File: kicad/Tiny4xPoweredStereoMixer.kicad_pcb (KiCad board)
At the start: 2 copper layers, 45 parts, among them J1 RCJ-2221, J2 RCJ-2221, J3 RCJ-2221, J4 RCJ-2221, J5 RCJ-2221, U1 TL072, U2 TL072, U3 TL072, U4 TL072, U5 TL072, U6 LM2611AMF/NOPB

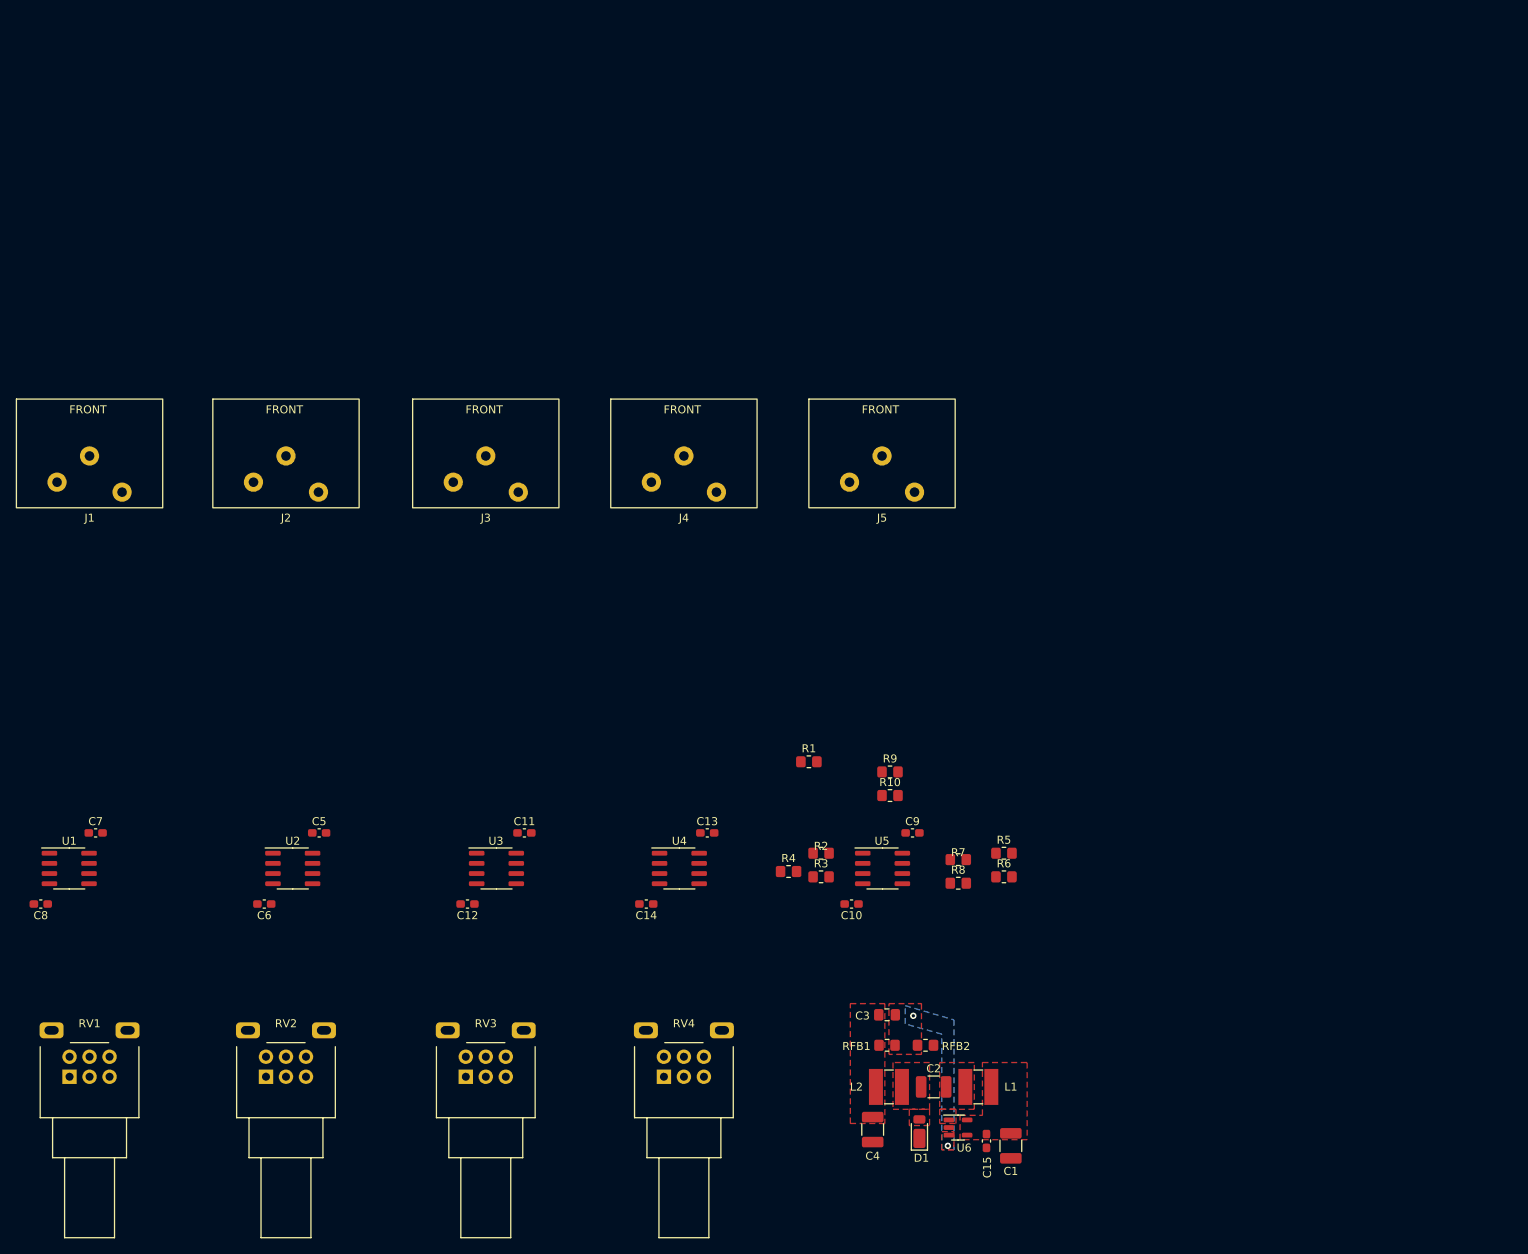
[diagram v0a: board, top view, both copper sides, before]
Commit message: positioned +/-12v connectors
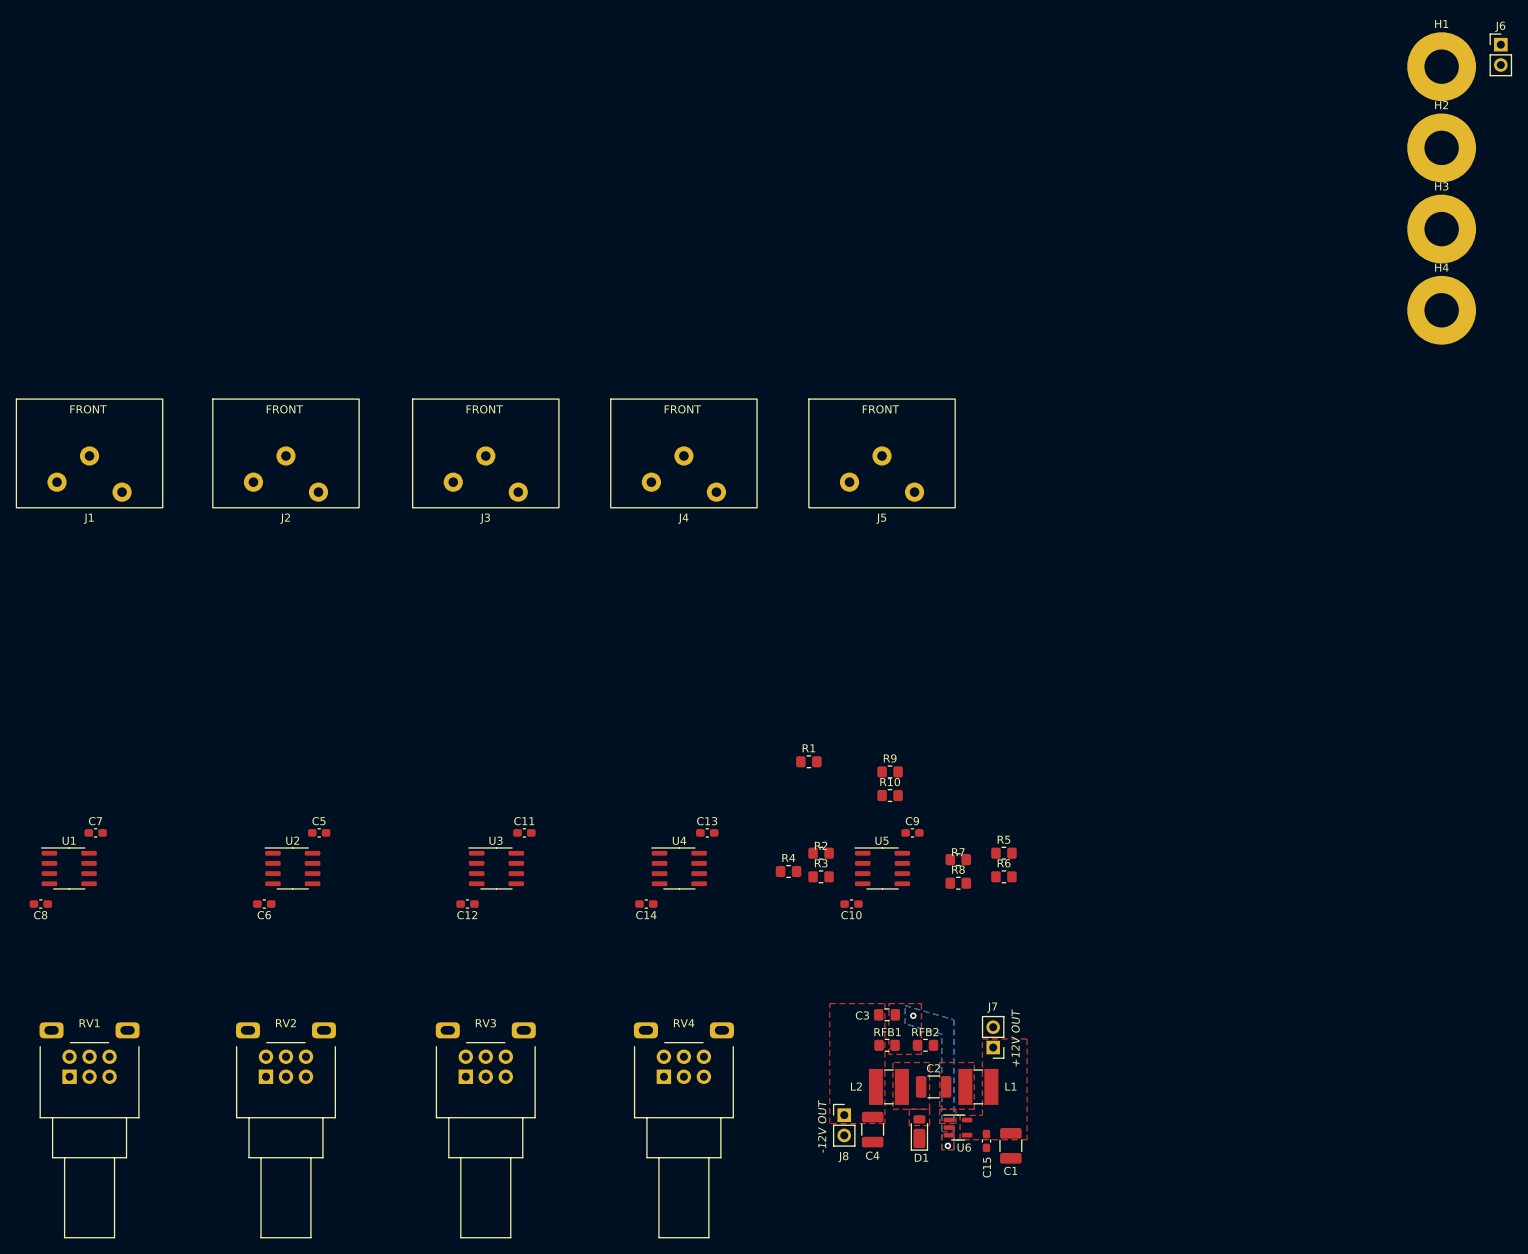
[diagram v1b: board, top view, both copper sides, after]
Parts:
- added H1: MountingHole, MountingHole:MountingHole_4.3mm_M4_Pad, F.Cu at (247.8, 23.6)
- added H2: MountingHole, MountingHole:MountingHole_4.3mm_M4_Pad, F.Cu at (247.8, 33.8)
- added H3: MountingHole, MountingHole:MountingHole_4.3mm_M4_Pad, F.Cu at (247.8, 43.9)
- added H4: MountingHole, MountingHole:MountingHole_4.3mm_M4_Pad, F.Cu at (247.8, 54.1)
- added J6: PowerConnector, Connector_PinHeader_2.54mm:PinHeader_1x02_P2.54mm_Vertical, F.Cu at (255.2, 20.9)
- added J7: PowerConnector, Connector_PinHeader_2.54mm:PinHeader_1x02_P2.54mm_Vertical, F.Cu at (191.7, 146.2)
- added J8: PowerConnector, Connector_PinHeader_2.54mm:PinHeader_1x02_P2.54mm_Vertical, F.Cu at (173.1, 154.7)
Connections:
- C1 pad 2: +12V -> Net-(J6-Pin_2)
- C15 pad 1: +12V -> Net-(J6-Pin_2)
- C3 pad 2: -12V -> Net-(J8-Pin_1)
- C4 pad 2: -12V -> Net-(J8-Pin_1)
- L1 pad 1: +12V -> Net-(J6-Pin_2)
- L2 pad 2: -12V -> Net-(J8-Pin_1)
- RFB1 pad 1: -12V -> Net-(J8-Pin_1)
- U6 pad 4: +12V -> Net-(J6-Pin_2)
- U6 pad 5: +12V -> Net-(J6-Pin_2)
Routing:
- added copper zone on F.Cu, net Net-(J6-Pin_2)
- added copper zone on F.Cu, net Net-(J8-Pin_1)
- removed copper zone on F.Cu, net +12V
- removed copper zone on F.Cu, net -12V

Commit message: completed reva layout
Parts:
- H1, H2, H3, H4: footprint MountingHole:MountingHole_4.3mm_M4_Pad -> MountingHole:MountingHole_3mm
- J1, J2, J3, J4, J5: footprint RCAJack:RCJ-22 -> RCAJack:CUI_DEVICES_RCJ-2211
- RV1, RV2, RV3, RV4: footprint Potentiometer_THT:Potentiometer_Alps_RK09L_Double_Horizontal -> Potentiometers:Potentiometer_Alps_RK09L_Double_Horizontal
- moved H2 180.1 mm to (100.3, 137.2)
- moved H3 163.4 mm to (104.1, 121.9)
- moved J6 154.8 mm to (170.4, 150.4), turned to 90 degrees
- moved H1 145.9 mm to (156.2, 137.2)
- moved H4 124.4 mm to (143.5, 121.9)
- moved J1 37.3 mm to (93.8, 105.3)
- moved J2 35.7 mm to (113.5, 105.3)
- moved J5 34.5 mm to (172.7, 105.3)
- moved J3 34.5 mm to (133.3, 105.3)
- moved J4 34.2 mm to (153.0, 105.3)
- moved R6 27.6 mm to (165.8, 120.1)
- moved R5 27.2 mm to (165.8, 122.4)
- moved C8 24.8 mm to (97.0, 123.2), turned to 0 degrees
- moved R8 23.7 mm to (165.8, 115.6)
- moved J8 22.3 mm to (161.9, 135.4), turned to 180 degrees
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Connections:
- R1 pad 1: /BufferOpAmp1/left_channel_buffered -> /BufferOpAmp4/left_channel_buffered
- R2 pad 1: /BufferOpAmp2/left_channel_buffered -> /BufferOpAmp3/left_channel_buffered
- R3 pad 1: /BufferOpAmp3/left_channel_buffered -> /BufferOpAmp2/left_channel_buffered
- R4 pad 1: /BufferOpAmp4/left_channel_buffered -> /BufferOpAmp1/left_channel_buffered
- R5 pad 1: /BufferOpAmp1/right_channel_buffered -> /BufferOpAmp4/right_channel_buffered
- R6 pad 1: /BufferOpAmp2/right_channel_buffered -> /BufferOpAmp3/right_channel_buffered
- R7 pad 1: /BufferOpAmp3/right_channel_buffered -> /BufferOpAmp2/right_channel_buffered
- R8 pad 1: /BufferOpAmp4/right_channel_buffered -> /BufferOpAmp1/right_channel_buffered
- RV1 pad 1: Net-(U1A--) -> Net-(U1B--)
- RV1 pad 2: /BufferOpAmp1/left_channel_buffered -> /BufferOpAmp1/right_channel_buffered
- RV1 pad 4: Net-(U1B--) -> Net-(U1A--)
- RV1 pad 5: /BufferOpAmp1/right_channel_buffered -> /BufferOpAmp1/left_channel_buffered
- RV2 pad 1: Net-(U2A--) -> Net-(U2B--)
- RV2 pad 2: /BufferOpAmp2/left_channel_buffered -> /BufferOpAmp2/right_channel_buffered
- RV2 pad 4: Net-(U2B--) -> Net-(U2A--)
- RV2 pad 5: /BufferOpAmp2/right_channel_buffered -> /BufferOpAmp2/left_channel_buffered
- RV3 pad 1: Net-(U3A--) -> Net-(U3B--)
- RV3 pad 2: /BufferOpAmp3/left_channel_buffered -> /BufferOpAmp3/right_channel_buffered
- RV3 pad 4: Net-(U3B--) -> Net-(U3A--)
- RV3 pad 5: /BufferOpAmp3/right_channel_buffered -> /BufferOpAmp3/left_channel_buffered
- RV4 pad 1: Net-(U4A--) -> Net-(U4B--)
- RV4 pad 2: /BufferOpAmp4/left_channel_buffered -> /BufferOpAmp4/right_channel_buffered
- RV4 pad 4: Net-(U4B--) -> Net-(U4A--)
- RV4 pad 5: /BufferOpAmp4/right_channel_buffered -> /BufferOpAmp4/left_channel_buffered
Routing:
- net /BufferOpAmp1/left_channel_buffered: track 0.00 -> 111.5 mm, vias 0 -> 1
- net /BufferOpAmp1/right_channel_buffered: track 0.00 -> 92.7 mm, vias 0 -> 1
- net /BufferOpAmp2/left_channel_buffered: track 0.00 -> 89.4 mm, vias 0 -> 1
- net /BufferOpAmp2/right_channel_buffered: track 0.00 -> 71.2 mm, vias 0 -> 1
- net /BufferOpAmp3/left_channel_buffered: track 0.00 -> 68.1 mm, vias 0 -> 1
- net /BufferOpAmp4/left_channel_buffered: track 0.00 -> 54.6 mm, vias 0 -> 1
- net /BufferOpAmp3/right_channel_buffered: track 0.00 -> 49.7 mm, vias 0 -> 1
- net /BufferOpAmp4/right_channel_buffered: track 0.00 -> 36.1 mm, vias 0 -> 1
- net Net-(U1B--): track 0.00 -> 31.3 mm
- net Net-(U3B--): track 0.00 -> 30.6 mm
- net Net-(U2B--): track 0.00 -> 30.6 mm
- net Net-(U4B--): track 0.00 -> 28.3 mm
- net /MixerOpAmp/left_channel_mix_out: track 0.00 -> 26.0 mm
- net /MixerOpAmp/right_channel_mix_out: track 0.00 -> 24.5 mm
- net Net-(U3A--): track 0.00 -> 21.2 mm
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- added copper zone on In1.Cu, net +12V
- added copper zone on In2.Cu, net -12V
- added copper zone on B.Cu, net GND
- added copper zone on F.Cu, net GND
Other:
- board outline added: 99.1 x 56.5 mm
- copper layers 2 -> 4
- board text added: "Tiny 4x Powered Stereo Mixer RevA 11/24"

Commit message: updated cuk converter negative feedback resistors
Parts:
- RFB1: value 88.7k -> 22k
- RFB2: value 10k -> 2k2

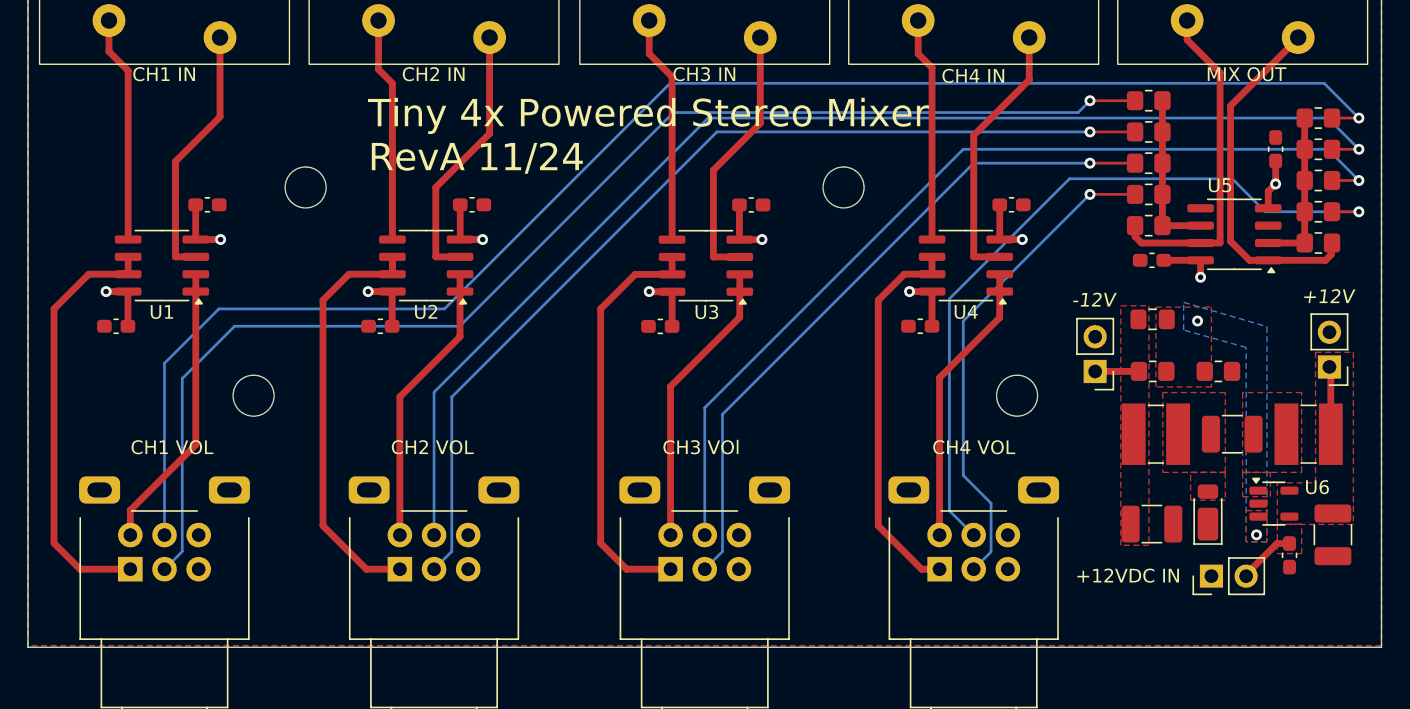
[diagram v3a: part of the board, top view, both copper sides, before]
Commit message: -  Fixed in-rush current problem using soft-start design. https://github.com/cracked-machine/Tiny4xPoweredStereoMixer/issues/4 - Fixed reversed pots. https://github.com/cracked-machine/Tiny4xPoweredStereoMixer/issues/3 - Made more space surrounding pwr in connector. https://github.com/cracked-machine/Tiny4xPoweredStereoMixer/issues/8
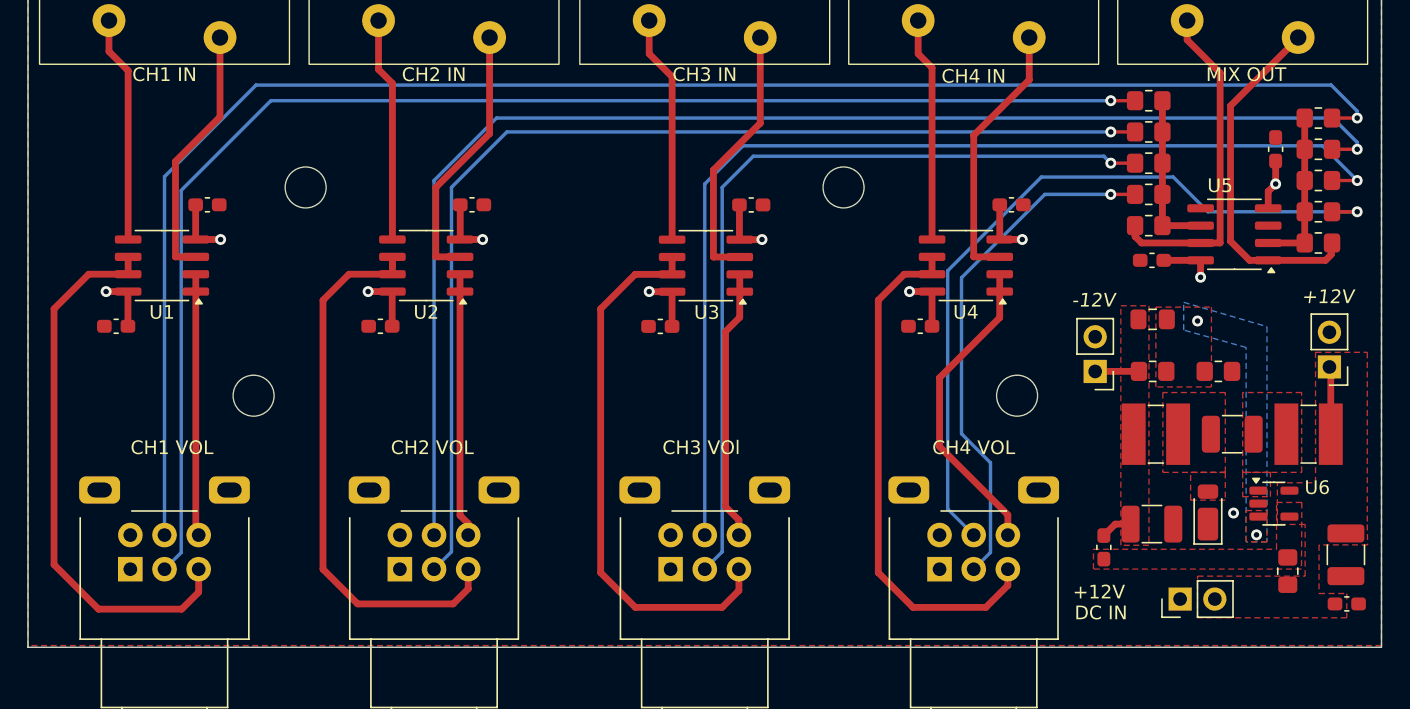
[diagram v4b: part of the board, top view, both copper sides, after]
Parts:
- added C16: 100nF, Capacitor_SMD:C_0603_1608Metric_Pad1.08x0.95mm_HandSolder, F.Cu at (162.6, 148.3)
- added R11: 100k, Resistor_SMD:R_0805_2012Metric_Pad1.20x1.40mm_HandSolder, F.Cu at (176.0, 150.0)
- moved C15 5.50 mm to (180.3, 152.4), turned to 0 degrees
- moved J6 2.84 mm to (168.1, 152.0)
- moved C1 1.74 mm to (180.3, 148.8)
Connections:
- RV1 pad 1: Net-(U1B--) -> GND
- RV1 pad 3: GND -> Net-(U1B--)
- RV1 pad 4: Net-(U1A--) -> GND
- RV1 pad 6: GND -> Net-(U1A--)
- RV2 pad 1: Net-(U2B--) -> GND
- RV2 pad 3: GND -> Net-(U2B--)
- RV2 pad 4: Net-(U2A--) -> GND
- RV2 pad 6: GND -> Net-(U2A--)
- RV3 pad 1: Net-(U3B--) -> GND
- RV3 pad 3: GND -> Net-(U3B--)
- RV3 pad 4: Net-(U3A--) -> GND
- RV3 pad 6: GND -> Net-(U3A--)
- RV4 pad 1: Net-(U4B--) -> GND
- RV4 pad 3: GND -> Net-(U4B--)
- RV4 pad 4: Net-(U4A--) -> GND
- RV4 pad 6: GND -> Net-(U4A--)
- U6 pad 4: Net-(J6-Pin_2) -> Net-(U6-~{SHDN})
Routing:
- net /BufferOpAmp3/right_channel_buffered: track 49.7 -> 59.8 mm
- net Net-(U4B--): track 28.3 -> 38.3 mm
- net Net-(U2B--): track 30.6 -> 40.4 mm
- net Net-(U3B--): track 30.6 -> 40.1 mm
- net /BufferOpAmp3/left_channel_buffered: track 68.1 -> 77.5 mm
- net Net-(U1B--): track 31.3 -> 40.6 mm
- net /BufferOpAmp2/left_channel_buffered: track 89.4 -> 98.5 mm
- net /BufferOpAmp2/right_channel_buffered: track 71.2 -> 80.2 mm
- net /BufferOpAmp1/right_channel_buffered: track 92.7 -> 100.8 mm
- net /BufferOpAmp1/left_channel_buffered: track 111.5 -> 119.4 mm
- net Net-(J6-Pin_2): track 9.20 -> 4.96 mm
- net Net-(J8-Pin_1): track 3.59 -> 5.89 mm
- net Net-(U4A--): track 20.9 -> 23.0 mm
- net Net-(U1A--): track 21.1 -> 19.2 mm
- net /BufferOpAmp4/right_channel_buffered: track 36.1 -> 37.9 mm
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- added copper zone on F.Cu, net Net-(U6-~{SHDN})
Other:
- board text added: "Tiny 4x Powered Stereo Mixer Rev${REVISION} ${ISSUE_DATE}"
- board text removed: "Tiny 4x Powered Stereo Mixer RevA 11/24"

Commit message: Refactored schematic into single page (except PSU)
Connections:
- net /BufferOpAmp1/left_channel_buffered renamed /ch1_left_mix_in
- net /BufferOpAmp1/left_channel_input renamed Net-(J1-Pin_3)
- net /BufferOpAmp1/right_channel_buffered renamed /ch1_right_mix_in
- net /BufferOpAmp1/right_channel_input renamed Net-(J1-Pin_2)
- net /BufferOpAmp2/left_channel_buffered renamed /ch2_left_mix_in
- net /BufferOpAmp2/left_channel_input renamed Net-(J2-Pin_3)
- net /BufferOpAmp2/right_channel_buffered renamed /ch2_right_mix_in
- net /BufferOpAmp2/right_channel_input renamed Net-(J2-Pin_2)
- net /BufferOpAmp3/left_channel_buffered renamed /ch3_left_mix_in
- net /BufferOpAmp3/left_channel_input renamed Net-(J3-Pin_3)
- net /BufferOpAmp3/right_channel_buffered renamed /ch3_right_mix_in
- net /BufferOpAmp3/right_channel_input renamed Net-(J3-Pin_2)
- net /BufferOpAmp4/left_channel_buffered renamed /ch4_left_mix_in
- net /BufferOpAmp4/left_channel_input renamed Net-(J4-Pin_3)
- net /BufferOpAmp4/right_channel_buffered renamed /ch4_right_mix_in
- net /BufferOpAmp4/right_channel_input renamed Net-(J4-Pin_2)
- net /MixerOpAmp/left_channel_mix_out renamed Net-(J5-Pin_3)
- net /MixerOpAmp/right_channel_mix_out renamed Net-(J5-Pin_2)
